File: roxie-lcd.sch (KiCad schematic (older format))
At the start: 7 parts, among them J1 Arduino-NANO-33, J2 VESC, J3 TFT, J4 BUTTON_1, J5 BUTTON_2, J6 BUTTON_3, J7 SD

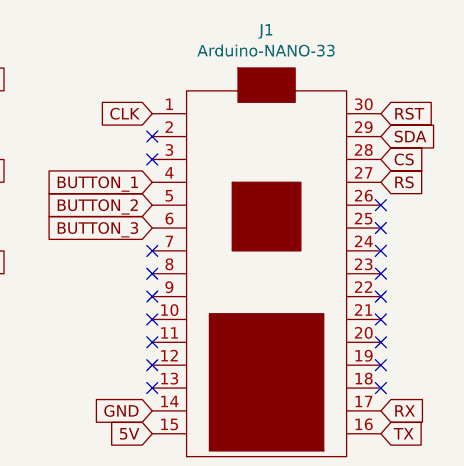
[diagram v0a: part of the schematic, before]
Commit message: changed position of connectors
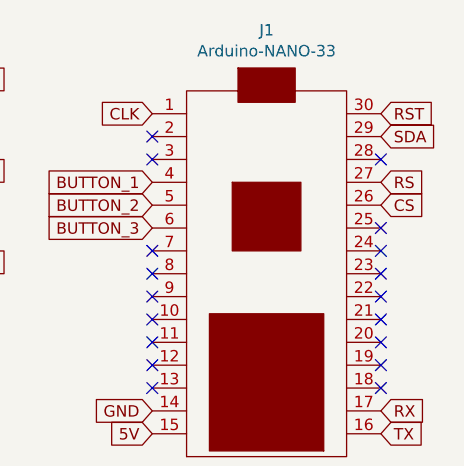
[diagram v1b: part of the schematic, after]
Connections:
- net CS: now also J1.26; no longer J1.28
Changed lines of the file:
@@
 Text GLabel 5500 1250 2    50   Input ~ 0
 RST
-Text GLabel 5500 1450 2    50   Input ~ 0
+Text GLabel 5500 1650 2    50   Input ~ 0
 CS
 Text GLabel 5500 1350 2    50   Input ~ 0
@@
 NoConn ~ 5500 1850
 NoConn ~ 5500 1750
-NoConn ~ 5500 1650
+NoConn ~ 5500 1450
 $Comp
 L Connector_Generic:Conn_01x04 J7

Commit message: first finished version
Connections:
- net 5V: now also J1.12; no longer J1.15
- net RST: now also J1.28; no longer J1.30
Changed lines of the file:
@@
 Text GLabel 4500 2550 0    50   Input ~ 0
 GND
-Text GLabel 4500 2650 0    50   Input ~ 0
+Text GLabel 4500 2350 0    50   Input ~ 0
 5V
 $Comp
@@
 Text GLabel 5500 1550 2    50   Input ~ 0
 RS
-Text GLabel 5500 1250 2    50   Input ~ 0
+Text GLabel 5500 1450 2    50   Input ~ 0
 RST
 Text GLabel 5500 1650 2    50   Input ~ 0
@@
 NoConn ~ 4500 2150
 NoConn ~ 4500 2250
-NoConn ~ 4500 2350
+NoConn ~ 4500 2650
 NoConn ~ 4500 2450
 NoConn ~ 5500 2450
@@
 NoConn ~ 5500 1850
 NoConn ~ 5500 1750
-NoConn ~ 5500 1450
+NoConn ~ 5500 1250
 $Comp
 L Connector_Generic:Conn_01x04 J7

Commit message: added mountingholes on pcb, added PDF's of schematic and PCB
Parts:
- added H1, H2, H3, H4: MountingHole, MountingHole:MountingHole_3.2mm_M3_ISO7380, symbol Mechanical:MountingHole
- J1: symbol Arduino-nano-33:Arduino-NANO-33 -> roxie-lcd-rescue:Arduino-NANO-33-Arduino-nano-33
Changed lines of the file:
@@
 $EndDescr
 $Comp
-L Arduino-nano-33:Arduino-NANO-33 J1
+L roxie-lcd-rescue:Arduino-NANO-33-Arduino-nano-33 J1
 U 1 1 5F116540
 P 5000 1950
@@
 EndData
 $EndBitmap
+$Comp
+L Mechanical:MountingHole H1
+U 1 1 5F23189F
+P 1200 5100
+F 0 "H1" H 1300 5146 50  0000 L CNN
+F 1 "MountingHole" H 1300 5055 50  0000 L CNN
+F 2 "MountingHole:MountingHole_3.2mm_M3_ISO7380" H 1200 5100 50  0001 C CNN
+F 3 "~" H 1200 5100 50  0001 C CNN
+	1    1200 5100
+	1    0    0    -1
+$EndComp
+$Comp
+L Mechanical:MountingHole H2
+U 1 1 5F231BE6
+P 1200 5350
+F 0 "H2" H 1300 5396 50  0000 L CNN
+F 1 "MountingHole" H 1300 5305 50  0000 L CNN
+F 2 "MountingHole:MountingHole_3.2mm_M3_ISO7380" H 1200 5350 50  0001 C CNN
+F 3 "~" H 1200 5350 50  0001 C CNN
+	1    1200 5350
+	1    0    0    -1
+$EndComp
+$Comp
+L Mechanical:MountingHole H3
+U 1 1 5F231F82
+P 1200 5600
+F 0 "H3" H 1300 5646 50  0000 L CNN
+F 1 "MountingHole" H 1300 5555 50  0000 L CNN
+F 2 "MountingHole:MountingHole_3.2mm_M3_ISO7380" H 1200 5600 50  0001 C CNN
+F 3 "~" H 1200 5600 50  0001 C CNN
+	1    1200 5600
+	1    0    0    -1
+$EndComp
+$Comp
+L Mechanical:MountingHole H4
+U 1 1 5F232494
+P 1200 5850
+F 0 "H4" H 1300 5896 50  0000 L CNN
+F 1 "MountingHole" H 1300 5805 50  0000 L CNN
+F 2 "MountingHole:MountingHole_3.2mm_M3_ISO7380" H 1200 5850 50  0001 C CNN
+F 3 "~" H 1200 5850 50  0001 C CNN
+	1    1200 5850
+	1    0    0    -1
+$EndComp
 $EndSCHEMATC

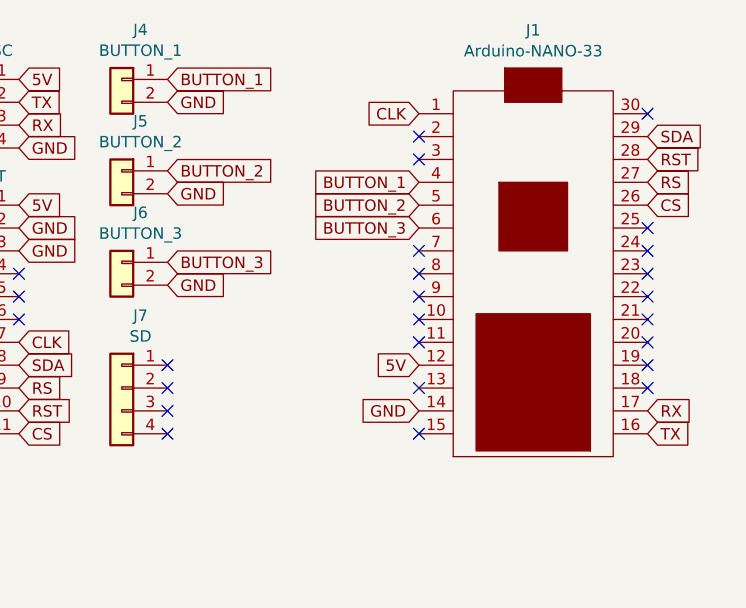
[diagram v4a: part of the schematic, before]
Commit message: Changed VESC connector to PH and added SD card support
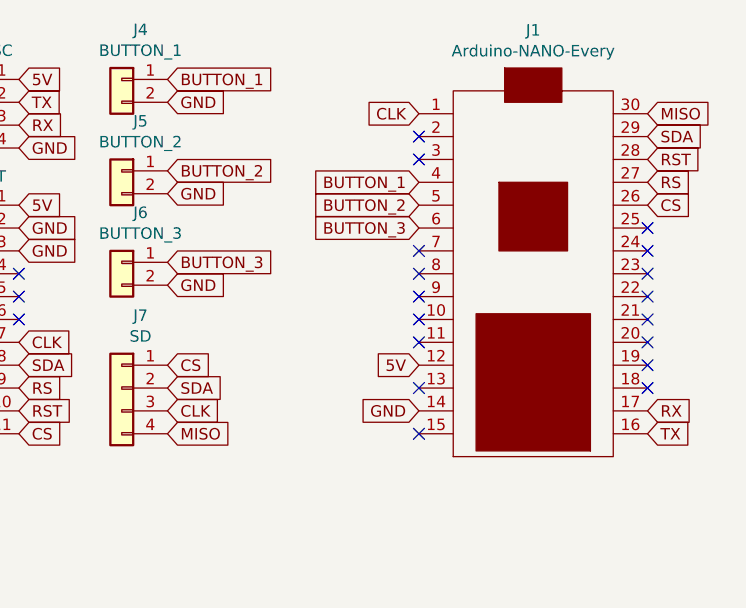
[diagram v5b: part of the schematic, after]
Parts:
- J1: value Arduino-NANO-33 -> Arduino-NANO-Every
- J2: footprint Connector_PinHeader_2.54mm:PinHeader_1x04_P2.54mm_Vertical -> Connector_JST:JST_PH_B4B-PH-K_1x04_P2.00mm_Vertical
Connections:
- net CLK: now also J7.3 (Pin_3)
- net CS: now also J7.1 (Pin_1)
- net SDA: now also J7.2 (Pin_2)
- net MISO: now reaches J1.30
- net MISO: now also J7.4 (Pin_4)
- no-connect marks 25 -> 20
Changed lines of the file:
@@
 P 5000 1950
 F 0 "J1" H 5000 3015 50  0000 C CNN
-F 1 "Arduino-NANO-33" H 5000 2924 50  0000 C CNN
+F 1 "Arduino-NANO-Every" H 5000 2924 50  0000 C CNN
 F 2 "lib:NANO_33_Footprint_SMD_Castell" H 4675 1850 50  0001 C CNN
 F 3 "~" H 4675 1850 50  0001 C CNN
@@
 Text GLabel 4500 2350 0    50   Input ~ 0
 5V
-$Comp
-L Connector_Generic:Conn_01x04 J2
-U 1 1 5F12737E
-P 2550 1200
-F 0 "J2" H 2468 1517 50  0000 C CNN
-F 1 "VESC" H 2468 1426 50  0000 C CNN
-F 2 "Connector_PinHeader_2.54mm:PinHeader_1x04_P2.54mm_Vertical" H 2550 1200 50  0001 C CNN
-F 3 "~" H 2550 1200 50  0001 C CNN
-	1    2550 1200
-	-1   0    0    -1
-$EndComp
 Text GLabel 2750 1300 2    50   Input ~ 0
 RX
@@
 NoConn ~ 5500 1850
 NoConn ~ 5500 1750
-NoConn ~ 5500 1250
 $Comp
 L Connector_Generic:Conn_01x04 J7
@@
 	-1   0    0    -1
 $EndComp
-NoConn ~ 3400 2350
-NoConn ~ 3400 2450
-NoConn ~ 3400 2550
-NoConn ~ 3400 2650
 $Comp
 L Mechanical:MountingHole H1
@@
 	1    0    0    -1
 $EndComp
+$Comp
+L Connector_Generic:Conn_01x04 J2
+U 1 1 5F12737E
+P 2550 1200
+F 0 "J2" H 2468 1517 50  0000 C CNN
+F 1 "VESC" H 2468 1426 50  0000 C CNN
+F 2 "Connector_JST:JST_PH_B4B-PH-K_1x04_P2.00mm_Vertical" H 2550 1200 50  0001 C CNN
+F 3 "~" H 2550 1200 50  0001 C CNN
+	1    2550 1200
+	-1   0    0    -1
+$EndComp
+Text GLabel 3400 2350 2    50   Input ~ 0
+CS
+Text GLabel 3400 2550 2    50   Input ~ 0
+CLK
+Text GLabel 3400 2450 2    50   Input ~ 0
+SDA
+Text GLabel 5500 1250 2    50   Input ~ 0
+MISO
+Text GLabel 3400 2650 2    50   Input ~ 0
+MISO
 $EndSCHEMATC
